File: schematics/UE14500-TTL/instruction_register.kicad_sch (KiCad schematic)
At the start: 12 parts, among them U1 74LS08, U2 74LS08, U3 74LS00, U4 74LS374, U5 74LS138, U6 74LS138

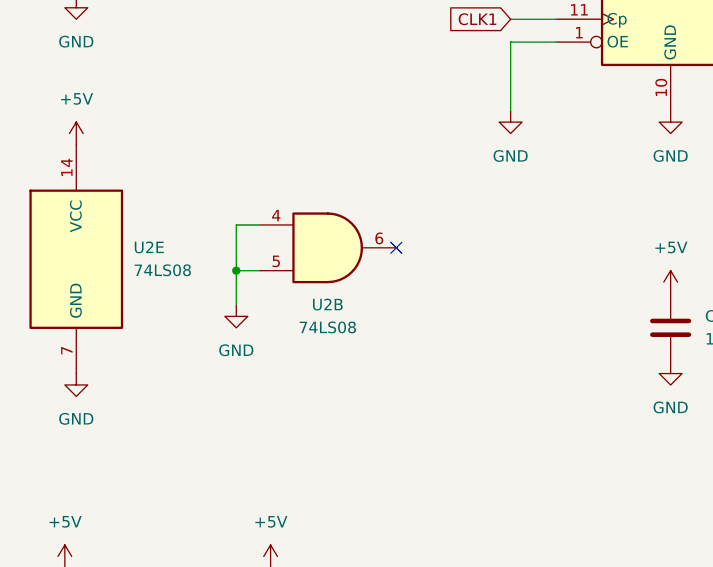
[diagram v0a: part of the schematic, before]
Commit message: Add a tape "REWIND" opcode to reset the PC early
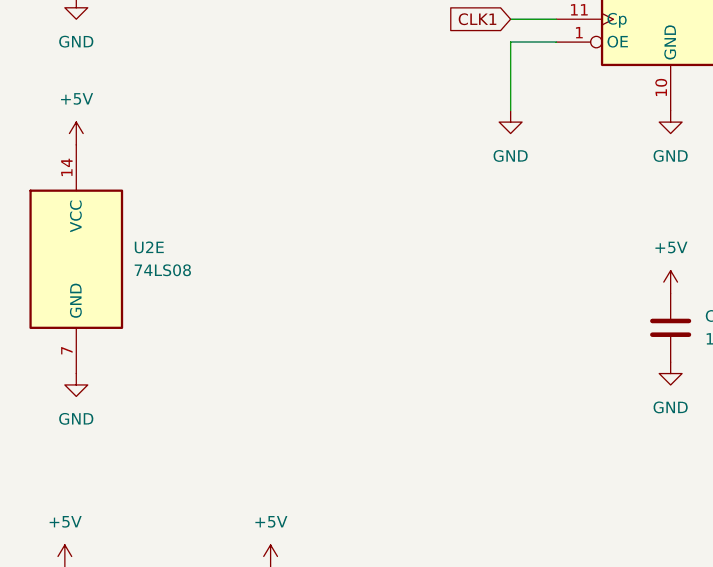
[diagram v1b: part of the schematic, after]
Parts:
- removed unit 2 of U2
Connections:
- no-connect marks 1 -> 0
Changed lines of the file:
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@@
 	)
 	(junction
-		(at 48.26 96.52)
-		(diameter 0)
-		(color 0 0 0 0)
-	)
-	(junction
 		(at 132.08 76.2)
 		(diameter 0)
 		(color 0 0 0 0)
 	)
-	(no_connect
-		(at 66.04 93.98)
-	)
 	(wire
 		(pts
@@
 	(wire
 		(pts
-			(xy 48.26 100.33) (xy 48.26 96.52)
-		)
-		(stroke
-			(width 0)
-			(type default)
-		)
-	)
-	(wire
-		(pts
 			(xy 182.88 83.82) (xy 182.88 76.2)
 		)
@@
 	(wire
 		(pts
-			(xy 48.26 91.44) (xy 50.8 91.44)
-		)
-		(stroke
-			(width 0)
-			(type default)
-		)
-	)
-	(wire
-		(pts
 			(xy 182.88 39.37) (xy 176.53 39.37)
 		)
@@
 	(wire
 		(pts
-			(xy 48.26 96.52) (xy 50.8 96.52)
-		)
-		(stroke
-			(width 0)
-			(type default)
-		)
-	)
-	(wire
-		(pts
 			(xy 173.99 63.5) (xy 185.42 63.5)
 		)
@@
 	(wire
 		(pts
-			(xy 48.26 96.52) (xy 48.26 91.44)
-		)
-		(stroke
-			(width 0)
-			(type default)
-		)
-	)
-	(wire
-		(pts
 			(xy 168.91 58.42) (xy 185.42 58.42)
 		)
@@
 	)
 	(symbol
-		(lib_id "74xx:74LS08")
-		(at 58.42 93.98 0)
-		(unit 2)
-		(exclude_from_sim no)
-		(in_bom yes)
-		(on_board yes)
-		(dnp no)
-		(property "Reference" "U2"
-			(at 58.42 100.33 0)
-			(effects
-				(font
-					(size 1.27 1.27)
-				)
-			)
-		)
-		(property "Value" "74LS08"
-			(at 58.42 102.87 0)
-			(effects
-				(font
-					(size 1.27 1.27)
-				)
-			)
-		)
-		(property "Footprint" "Package_DIP:DIP-14_W7.62mm"
-			(at 58.42 93.98 0)
-			(effects
-				(font
-					(size 1.27 1.27)
-				)
-				(hide yes)
-			)
-		)
-		(property "Datasheet" "http://www.ti.com/lit/gpn/sn74LS08"
-			(at 58.42 93.98 0)
-			(effects
-				(font
-					(size 1.27 1.27)
-				)
-				(hide yes)
-			)
-		)
-		(property "Description" "Quad And2"
-			(at 58.42 93.98 0)
-			(effects
-				(font
-					(size 1.27 1.27)
-				)
-				(hide yes)
-			)
-		)
-		(pin "7"
-		)
-		(pin "8"
-		)
-		(pin "5"
-		)
-		(pin "9"
-		)
-		(pin "10"
-		)
-		(pin "1"
-		)
-		(pin "3"
-		)
-		(pin "14"
-		)
-		(pin "2"
-		)
-		(pin "6"
-		)
-		(pin "11"
-		)
-		(pin "4"
-		)
-		(pin "12"
-		)
-		(pin "13"
-		)
-		(instances
-			(project "UE14500-TTL"
-				(path "/3387ba40-0694-43b2-a156-d12ce9552f1f/ae25e494-ab45-4d0a-a9ba-a92e3da9ec94"
-					(reference "U2")
-					(unit 2)
-				)
-			)
-		)
-	)
-	(symbol
 		(lib_id "power:GND")
 		(at 78.74 78.74 0)
@@
 					(unit 1)
 				)
-			)
-		)
-	)
-	(symbol
-		(lib_id "power:GND")
-		(at 48.26 100.33 0)
-		(unit 1)
-		(exclude_from_sim no)
-		(in_bom yes)
-		(on_board yes)
-		(dnp no)
-		(fields_autoplaced yes)
-		(property "Reference" "#PWR24"
-			(at 48.26 106.68 0)
-			(effects
-				(font
-					(size 1.27 1.27)
-				)
-				(hide yes)
-			)
-		)
-		(property "Value" "GND"
-			(at 48.26 105.41 0)
-			(effects
-				(font
-					(size 1.27 1.27)
-				)
-			)
-		)
-		(property "Footprint" ""
-			(at 48.26 100.33 0)
-			(effects
-				(font
-					(size 1.27 1.27)
-				)
-				(hide yes)
-			)
-		)
-		(property "Datasheet" ""
-			(at 48.26 100.33 0)
-			(effects
-				(font
-					(size 1.27 1.27)
-				)
-				(hide yes)
-			)
-		)
-		(property "Description" "Power symbol creates a global label with name \"GND\" , ground"
-			(at 48.26 100.33 0)
-			(effects
-				(font
-					(size 1.27 1.27)
-				)
-				(hide yes)
-			)
-		)
-		(pin "1"
-		)
-		(instances
-			(project "UE14500-TTL"
-				(path "/3387ba40-0694-43b2-a156-d12ce9552f1f/ae25e494-ab45-4d0a-a9ba-a92e3da9ec94"
-					(reference "#PWR24")
-					(unit 1)
-				)
